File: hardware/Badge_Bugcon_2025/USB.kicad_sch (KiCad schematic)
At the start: 33 parts, among them J3 USB_A, J4 USB_A, J6 USB_A, P4 USB_C_Plug_USB2.0, Q1 DMG3415U-7, SW1 ON, SW4 SWITCH, U1 USB3740B-AI9, U3 SL2.1A, Y5 12MHz

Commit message: feat(Hw):Update_Schematic
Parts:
- removed BT1, BT2, BT3: Battery_Cell, Battery:BatteryHolder_Keystone_2466_1xAAA, symbol Device:Battery_Cell
- added C70, C71: 4.7uF, symbol Device:C
- added D16: D, symbol Device:D
- added J10: Conn_01x02, symbol Connector_Generic:Conn_01x02
- added R31: 2k, symbol Device:R
- added R32: 470, symbol Device:R
- added U5: MCP73831T-2ATI/OT, Package_TO_SOT_SMD:SOT-23-5, symbol Battery_Management:MCP73831-2-OT
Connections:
- net +5V: no longer SW4.1 (A), U1.5 (VDD)
- net +BATT: now also J10.1 (Pin_1)
- net GND: now also C70.1, C71.2, J10.2 (Pin_2), R31.2, U5.2 (V_{SS})
- net VBUS: now also D14.2 (A), D15.2 (A), SW4.1 (A), U1.5 (VDD), C70.2, D16.2 (A), U5.4 (V_{DD}); no longer D14.1 (K), D15.1 (K)
- net at F4.1: now also D15.1 (K); no longer D15.2 (A)
- net at F3.1: now also D14.1 (K); no longer D14.2 (A)
- new net: C71.1, U5.3 (V_{BAT})
- new net: R31.1, U5.5 (PROG)
- new net: D16.1 (K), R32.1
- new net STAT: R32.2, U5.1 (STAT)
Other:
- moved on the sheet: C18, C19, C55, C56, C57, D12, D14, D15, F3, F4, J4, J6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

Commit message: feat(Hw):Update_Schematic
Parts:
- C19, C55: footprint (none) -> Capacitor_SMD:C_0603_1608Metric; LCSC# (none) -> C96446
- C56, C57: footprint (none) -> Capacitor_SMD:C_0603_1608Metric
- C70, C71: footprint (none) -> Capacitor_SMD:C_0603_1608Metric; LCSC# (none) -> C162274
- D16: value D -> LED; footprint (none) -> LED_SMD:LED_0603_1608Metric; LCSC# (none) -> C375573
- J3, J4, J6: LCSC# (none) -> C18077686
- U3: LCSC# (none) -> C192893
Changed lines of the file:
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@@
 			)
 		)
-		(property "Value" "D"
+		(property "Value" "LED"
 			(at 262.89 73.6599 90)
 			(effects
@@
 			)
 		)
-		(property "Footprint" ""
+		(property "Footprint" "LED_SMD:LED_0603_1608Metric"
 			(at 260.35 72.39 0)
 			(effects
@@
 			)
 		)
+		(property "LCSC#" "C375573"
+			(at 260.35 72.39 90)
+			(effects
+				(font
+					(size 1.27 1.27)
+				)
+				(hide yes)
+			)
+		)
 		(pin "2"
 		)
@@
 			)
 		)
+		(property "LCSC#" "C18077686"
+			(at 27.94 116.84 0)
+			(effects
+				(font
+					(size 1.27 1.27)
+				)
+				(hide yes)
+			)
+		)
 		(pin "1"
 		)
@@
 			)
 		)
+		(property "LCSC#" "C192893"
+			(at 90.17 156.21 0)
+			(effects
+				(font
+					(size 1.27 1.27)
+				)
+				(hide yes)
+			)
+		)
 		(pin "7"
 		)
@@
 			)
 		)
-		(property "Footprint" ""
+		(property "Footprint" "Capacitor_SMD:C_0603_1608Metric"
 			(at 242.2652 82.55 0)
 			(effects
@@
 			)
 		)
+		(property "LCSC#" "C162274"
+			(at 241.3 78.74 0)
+			(effects
+				(font
+					(size 1.27 1.27)
+				)
+				(hide yes)
+			)
+		)
 		(pin "1"
 		)
@@
 			)
 		)
-		(property "Footprint" ""
+		(property "Footprint" "Capacitor_SMD:C_0603_1608Metric"
 			(at 63.8048 162.56 0)
 			(effects
@@
 			)
 		)
+		(property "LCSC#" "C96446"
+			(at 64.77 166.37 0)
+			(effects
+				(font
+					(size 1.27 1.27)
+				)
+				(hide yes)
+			)
+		)
 		(pin "2"
 		)
@@
 			)
 		)
-		(property "Footprint" ""
+		(property "Footprint" "Capacitor_SMD:C_0603_1608Metric"
 			(at 58.1152 170.18 0)
 			(effects
@@
 			)
 		)
+		(property "LCSC#" "C96446"
+			(at 57.15 166.37 0)
+			(effects
+				(font
+					(size 1.27 1.27)
+				)
+				(hide yes)
+			)
+		)
 		(pin "1"
 		)
@@
 			)
 		)
-		(property "Footprint" ""
+		(property "Footprint" "Capacitor_SMD:C_0603_1608Metric"
 			(at 159.7152 140.97 0)
 			(effects
@@
 			)
 		)
-		(property "Footprint" ""
+		(property "Footprint" "Capacitor_SMD:C_0603_1608Metric"
 			(at 210.82 62.5348 0)
 			(effects
@@
 			)
 		)
+		(property "LCSC#" "C162274"
+			(at 207.01 63.5 90)
+			(effects
+				(font
+					(size 1.27 1.27)
+				)
+				(hide yes)
+			)
+		)
 		(pin "1"
 		)
@@
 			)
 		)
-		(property "Footprint" ""
+		(property "Footprint" "Capacitor_SMD:C_0603_1608Metric"
 			(at 160.9852 173.99 0)
 			(effects
@@
 			)
 		)
+		(property "LCSC#" "C18077686"
+			(at 144.78 137.16 0)
+			(effects
+				(font
+					(size 1.27 1.27)
+				)
+				(hide yes)
+			)
+		)
 		(pin "1"
 		)
@@
 			(at 144.78 170.18 0)
 			(effects
+				(font
+					(size 1.27 1.27)
+				)
+				(hide yes)
+			)
+		)
+		(property "LCSC#" "C18077686"
+			(at 144.78 170.18 0)
+			(effects

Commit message: feat(Hw):Update_BOM
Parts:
- removed SW4: SWITCH, symbol Switch:SW_SPDT
- added SW4: On, Footprints:MSK12C02, symbol Switch:SW_DPDT_x2
- C56, C57: footprint Capacitor_SMD:C_0603_1608Metric -> Capacitor_SMD:C_0805_2012Metric; LCSC# (none) -> C141660
- J3, J4, J6: footprint (none) -> Connector_USB:USB_A_Connfly_DS1095
- R31: footprint (none) -> LED_SMD:LED_0603_1608Metric; LCSC# (none) -> C2907022
- R32: footprint (none) -> LED_SMD:LED_0603_1608Metric; LCSC# (none) -> C23179
- U1: footprint (none) -> Package_DFN_QFN:UQFN-10_1.3x1.8mm_P0.4mm
- U3: footprint (none) -> Package_SO:SOP-16_3.9x9.9mm_P1.27mm
- Y5: footprint Crystal:Crystal_SMD_3215-2Pin_3.2x1.5mm -> Crystal:Crystal_SMD_3225-4Pin_3.2x2.5mm; LCSC# C620155 -> C133334
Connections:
- net GND: now also SW4.3 (C), SW4.4 (C)
- net S: now also SW4.2 (B)
- net VBUS: now also SW4.1 (A)
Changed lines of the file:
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@@
 	)
 	(junction
+		(at 165.1 49.53)
+		(diameter 0)
+		(color 0 0 0 0)
+	)
+	(junction
 		(at 146.05 181.61)
 		(diameter 0)
@@
 	(wire
 		(pts
+			(xy 162.56 45.72) (xy 165.1 45.72)
+		)
+		(stroke
+			(width 0)
+			(type default)
+		)
+	)
+	(wire
+		(pts
 			(xy 215.9 83.82) (xy 215.9 85.09)
 		)
@@
 	(wire
 		(pts
+			(xy 165.1 45.72) (xy 165.1 49.53)
+		)
+		(stroke
+			(width 0)
+			(type default)
+		)
+	)
+	(wire
+		(pts
 			(xy 135.89 132.08) (xy 137.16 132.08)
 		)
@@
 	(wire
 		(pts
-			(xy 165.1 45.72) (xy 162.56 45.72)
+			(xy 165.1 49.53) (xy 162.56 49.53)
 		)
 		(stroke
@@
 	(wire
 		(pts
-			(xy 165.1 46.99) (xy 165.1 45.72)
+			(xy 165.1 52.07) (xy 165.1 49.53)
 		)
 		(stroke
@@
 	(symbol
 		(lib_id "power:GND")
-		(at 165.1 46.99 0)
+		(at 165.1 52.07 0)
 		(unit 1)
 		(exclude_from_sim no)
@@
 		(dnp no)
 		(property "Reference" "#PWR086"
-			(at 165.1 53.34 0)
+			(at 165.1 58.42 0)
 			(effects
 				(font
@@
 		)
 		(property "Value" "GND"
-			(at 165.227 51.3842 0)
+			(at 165.227 56.4642 0)
 			(effects
 				(font
@@
 		)
 		(property "Footprint" ""
-			(at 165.1 46.99 0)
+			(at 165.1 52.07 0)
 			(effects
 				(font
@@
 		)
 		(property "Datasheet" ""
-			(at 165.1 46.99 0)
+			(at 165.1 52.07 0)
 			(effects
 				(font
@@
 		)
 		(property "Description" ""
-			(at 165.1 46.99 0)
+			(at 165.1 52.07 0)
 			(effects
 				(font
@@
 			)
 		)
-		(property "Footprint" ""
+		(property "Footprint" "Connector_USB:USB_A_Connfly_DS1095"
 			(at 31.75 118.11 0)
 			(effects
@@
 			)
 		)
-		(property "Footprint" ""
+		(property "Footprint" "Package_SO:SOP-16_3.9x9.9mm_P1.27mm"
 			(at 90.17 156.21 0)
 			(effects
@@
 			)
 		)
-		(property "Footprint" ""
+		(property "Footprint" "Package_DFN_QFN:UQFN-10_1.3x1.8mm_P0.4mm"
 			(at 90.17 49.53 0)
 			(effects
@@
 			)
 		)
-		(property "Footprint" ""
+		(property "Footprint" "LED_SMD:LED_0603_1608Metric"
 			(at 258.572 81.28 90)
 			(effects
@@
 			)
 		)
+		(property "LCSC#" "C23179"
+			(at 260.35 81.28 0)
+			(effects
+				(font
+					(size 1.27 1.27)
+				)
+				(hide yes)
+			)
+		)
 		(pin "2"
 		)
@@
 	)
 	(symbol
+		(lib_id "Switch:SW_DPDT_x2")
+		(at 157.48 43.18 0)
+		(unit 1)
+		(exclude_from_sim no)
+		(in_bom yes)
+		(on_board yes)
+		(dnp no)
+		(property "Reference" "SW4"
+			(at 155.702 46.609 0)
+			(effects
+				(font
+					(size 1.27 1.27)
+				)
+			)
+		)
+		(property "Value" "On"
+			(at 157.48 38.2524 0)
+			(effects
+				(font
+					(size 1.27 1.27)
+				)
+			)
+		)
+		(property "Footprint" "Footprints:MSK12C02"
+			(at 157.48 43.18 0)
+			(effects
+				(font
+					(size 1.27 1.27)
+				)
+				(hide yes)
+			)
+		)
+		(property "Datasheet" "~"
+			(at 157.48 43.18 0)
+			(effects
+				(font
+					(size 1.27 1.27)
+				)
+				(hide yes)
+			)
+		)
+		(property "Description" ""
+			(at 157.48 43.18 0)
+			(effects
+				(font
+					(size 1.27 1.27)
+				)
+				(hide yes)
+			)
+		)
+		(property "LCSC#" "C431540"
+			(at 157.48 43.18 0)
+			(effects
+				(font
+					(size 1.27 1.27)
+				)
+				(hide yes)
+			)
+		)
+		(property "manf#" ""
+			(at 157.48 43.18 0)
+			(effects
+				(font
+					(size 1.27 1.27)
+				)
+				(hide yes)
+			)
+		)
+		(pin "1"
+		)
+		(pin "2"
+		)
+		(pin "3"
+		)
+		(pin "4"
+		)
+		(pin "5"
+		)
+		(pin "6"
+		)
+		(pin "4"
+		)
+		(instances
+			(project "Badge_Bugcon_2025"
+				(path "/a95785a0-0aa1-454e-b59f-0ac64970ac71/a5c26cac-72fa-4752-a660-9cd751934916"
+					(reference "SW4")
+					(unit 1)
+				)
+			)
+		)
+	)
+	(symbol
 		(lib_id "power:GND")
 		(at 49.53 157.48 0)
@@
 	)
 	(symbol
-		(lib_id "Switch:SW_SPDT")
-		(at 157.48 43.18 0)
-		(unit 1)
-		(exclude_from_sim no)
-		(in_bom yes)
-		(on_board yes)
-		(dnp no)
-		(fields_autoplaced yes)
-		(property "Reference" "SW4"
-			(at 157.48 34.29 0)
-			(effects
-				(font
-					(size 1.27 1.27)
-				)
-			)
-		)
-		(property "Value" "SWITCH"
-			(at 157.48 36.83 0)
-			(effects
-				(font
-					(size 1.27 1.27)
-				)
-			)
-		)
-		(property "Footprint" ""
-			(at 157.48 43.18 0)
-			(effects
-				(font
-					(size 1.27 1.27)
-				)
-				(hide yes)
-			)
-		)
-		(property "Datasheet" "~"
-			(at 157.48 50.8 0)
-			(effects
-				(font
-					(size 1.27 1.27)
-				)
-				(hide yes)
-			)
-		)
-		(property "Description" "Switch, single pole double throw"
-			(at 157.48 43.18 0)
-			(effects
-				(font
-					(size 1.27 1.27)
-				)
-				(hide yes)
-			)
-		)
-		(property "Height" ""
-			(at 157.48 43.18 0)
-			(effects
-				(font
-					(size 1.27 1.27)
-				)
-				(hide yes)
-			)
-		)
-		(property "Manufacturer_Name" ""
-			(at 157.48 43.18 0)
-			(effects
-				(font
-					(size 1.27 1.27)
-				)
-				(hide yes)
-			)
-		)
-		(property "Mouser Part Number" ""
-			(at 157.48 43.18 0)
-			(effects
-				(font
-					(size 1.27 1.27)
-				)
-				(hide yes)
-			)
-		)
-		(property "Mouser Price/Stock" ""
-			(at 157.48 43.18 0)
-			(effects
-				(font
-					(size 1.27 1.27)
-				)
-				(hide yes)
-			)
-		)
-		(pin "3"
-		)
-		(pin "1"
-		)
-		(pin "2"
-		)
-		(instances
-			(project ""
-				(path "/a95785a0-0aa1-454e-b59f-0ac64970ac71/a5c26cac-72fa-4752-a660-9cd751934916"
-					(reference "SW4")
-					(unit 1)
-				)
-			)
-		)
-	)
-	(symbol
 		(lib_id "power:+5V")
 		(at 243.84 139.7 0)
@@
 			)
 		)
-		(property "Footprint" "Capacitor_SMD:C_0603_1608Metric"
+		(property "Footprint" "Capacitor_SMD:C_0805_2012Metric"
 			(at 159.7152 140.97 0)
 			(effects
@@
 			)
 		)
+		(property "LCSC#" "C141660"
+			(at 158.75 137.16 0)
+			(effects
+				(font
+					(size 1.27 1.27)
+				)
+				(hide yes)
+			)
+		)
 		(pin "1"
 		)
@@
 			)
 		)
-		(property "Footprint" "Capacitor_SMD:C_0603_1608Metric"
+		(property "Footprint" "Capacitor_SMD:C_0805_2012Metric"
 			(at 160.9852 173.99 0)
 			(effects
@@
 			)
 		)
+		(property "LCSC#" "C141660"
+			(at 160.02 170.18 0)
+			(effects
+				(font
+					(size 1.27 1.27)
+				)
+				(hide yes)
+			)
+		)
 		(pin "1"
 		)
@@
 			)
 		)
-		(property "Footprint" ""
+		(property "Footprint" "Connector_USB:USB_A_Connfly_DS1095"
 			(at 140.97 138.43 0)
 			(effects
@@
 			)
 		)
-		(property "Footprint" ""
+		(property "Footprint" "LED_SMD:LED_0603_1608Metric"
 			(at 197.612 83.82 90)
 			(effects
@@
 			)
 		)
+		(property "LCSC#" "C2907022"
+			(at 199.39 83.82 0)
+			(effects
+				(font
+					(size 1.27 1.27)
+				)
+				(hide yes)
+			)
+		)
 		(pin "1"
 		)
@@
 			)
 		)
-		(property "Footprint" ""
+		(property "Footprint" "Connector_USB:USB_A_Connfly_DS1095"
 			(at 140.97 171.45 0)
 			(effects
@@
 			)
 		)
-		(property "Footprint" "Crystal:Crystal_SMD_3215-2Pin_3.2x1.5mm"
+		(property "Footprint" "Crystal:Crystal_SMD_3225-4Pin_3.2x2.5mm"
 			(at 83.82 184.15 0)
 			(effects
@@
 			)
 		)
-		(property "LCSC#" "C620155"
+		(property "LCSC#" "C133334"
 			(at 83.82 184.15 0)
 			(effects

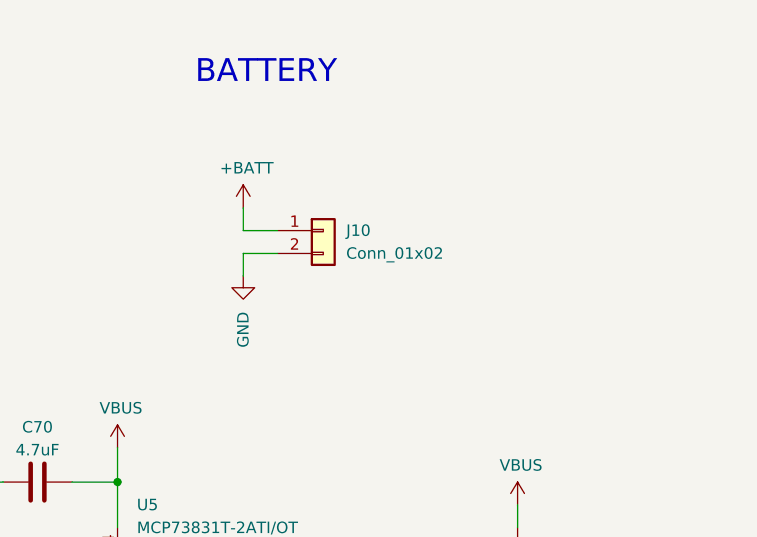
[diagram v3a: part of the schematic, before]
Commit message: feat(Hw):Update_Schematic_And_Floorplan
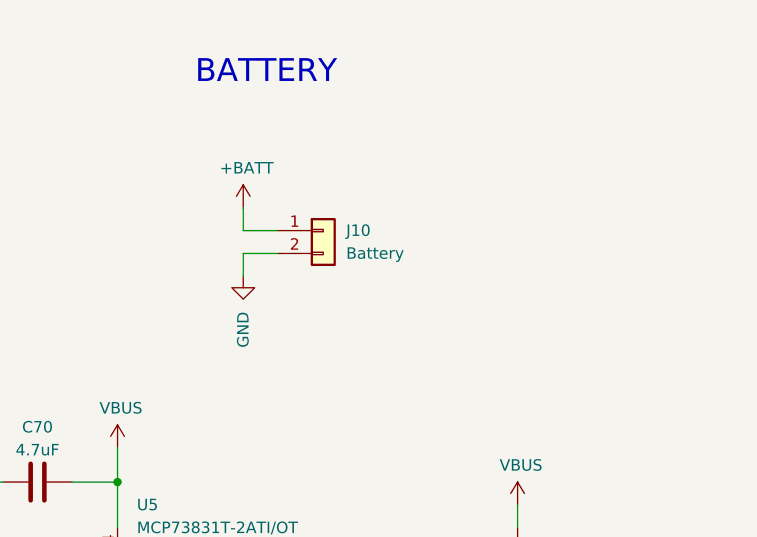
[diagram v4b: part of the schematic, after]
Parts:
- J10: value Conn_01x02 -> Battery; footprint (none) -> Footprints:Batt; LCSC# (none) -> C131337
- SW1: footprint FootprintsB:SW-TH_SK12D07VG4 -> Button_Switch_THT:SW_Slide_SPDT_Angled_CK_OS102011MA1Q
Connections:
- net XIN: now also Y5.3; no longer Y5.2
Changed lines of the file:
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@@
 			)
 		)
-		(property "Value" "Conn_01x02"
+		(property "Value" "Battery"
 			(at 241.3 38.0999 0)
 			(effects
@@
 			)
 		)
-		(property "Footprint" ""
+		(property "Footprint" "Footprints:Batt"
 			(at 238.76 35.56 0)
 			(effects
@@
 			)
 		)
-		(property "Datasheet" "https://uelectronics.com/producto/bateria-lipo-3-7v-2500mah/"
+		(property "Datasheet" ""
 			(at 238.76 35.56 0)
 			(effects
@@
 			)
 		)
+		(property "LCSC#" "C131337"
+			(at 238.76 35.56 0)
+			(effects
+				(font
+					(size 1.27 1.27)
+				)
+				(hide yes)
+			)
+		)
 		(pin "2"
 		)
@@
 			)
 		)
-		(property "Footprint" "FootprintsB:SW-TH_SK12D07VG4"
+		(property "Footprint" "Button_Switch_THT:SW_Slide_SPDT_Angled_CK_OS102011MA1Q"
 			(at 229.87 142.24 0)
 			(effects
@@
 		(pin "1"
 		)
-		(pin "2"
+		(pin "3"
 		)
 		(instances

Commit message: feat(Hw):Update_Schematic
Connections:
- net +BATT: now also C71.1, U5.3 (V_{BAT})
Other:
- note added: "BATTERY CHARGER"
- note added: "USB SELECTOR"
- note removed: "BATTERY"
- moved on the sheet: C18, C19, C54, C55, C56, C57, C70, C71, D12, D13, D14, D15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

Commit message: feat(Hw):Update_Schematic
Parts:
- removed U5: MCP73831T-2ATI/OT, Package_TO_SOT_SMD:SOT-23-5, symbol Battery_Management:MCP73831-2-OT
- added D8: LED, LED_SMD:LED_0603_1608Metric, symbol Device:D
- added U2: TP4056, Package_SO:SOIC-8-1EP_3.9x4.9mm_P1.27mm_EP2.41x3.3mm_ThermalVias, symbol Battery_Management:TP4056-42-ESOP8
- C70, C71: value 4.7uF -> 10uF
- R32: value 470 -> 10K; footprint LED_SMD:LED_0603_1608Metric -> Resistor_SMD:R_0402_1005Metric; LCSC# C23179 -> C2759535
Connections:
- net STAT is gone; now on net GND: R32.2
- net +BATT: now also U2.5 (BAT)
- net GND: now also U2.3 (GND), U2.9 (EPAD); no longer R31.2
- net VBUS: now also R31.1, U2.4 (V_{CC}); no longer D16.2 (A)
- net at D16.1 (K): now also U2.7 (~{CHRG}); no longer R32.1
- new net: D16.2 (A), D8.2 (A), R31.2
- new net: R32.1, U2.2 (PROG)
- new net: D8.1 (K), U2.6 (~{STDBY})
- no-connect marks 4 -> 5
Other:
- moved on the sheet: C70, C71, D16, R31

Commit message: feat(Hw):Update_Schematic
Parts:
- C70, C71: LCSC# C162274 -> C96446
- J10: LCSC# C131337 -> C2988620; manf# Bateria LiPo 3.7V 2500mAh 104050 -> Bateria 18650 3.7V 2200mAh ±5%
- U2: LCSC# (none) -> C725790
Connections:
- net VBUS: now also U2.8 (CE)
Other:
- moved on the sheet: C70
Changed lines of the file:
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@@
 	)
 	(junction
-		(at 218.44 48.26)
+		(at 218.44 44.45)
 		(diameter 0)
 		(color 0 0 0 0)
@@
 	)
 	(junction
+		(at 218.44 52.07)
+		(diameter 0)
+		(color 0 0 0 0)
+	)
+	(junction
 		(at 186.69 66.04)
 		(diameter 0)
@@
 	(wire
 		(pts
-			(xy 213.36 48.26) (xy 218.44 48.26)
+			(xy 213.36 44.45) (xy 218.44 44.45)
 		)
 		(stroke
@@
 	(wire
 		(pts
-			(xy 205.74 48.26) (xy 203.2 48.26)
+			(xy 205.74 44.45) (xy 203.2 44.45)
 		)
 		(stroke
@@
 	(wire
 		(pts
+			(xy 218.44 52.07) (xy 218.44 53.34)
+		)
+		(stroke
+			(width 0)
+			(type default)
+		)
+	)
+	(wire
+		(pts
 			(xy 142.24 22.86) (xy 143.51 22.86)
 		)
@@
 	(wire
 		(pts
-			(xy 218.44 44.45) (xy 218.44 48.26)
+			(xy 218.44 39.37) (xy 218.44 44.45)
 		)
 		(stroke
@@
 	(wire
 		(pts
-			(xy 218.44 48.26) (xy 218.44 53.34)
+			(xy 218.44 44.45) (xy 218.44 52.07)
 		)
 		(stroke
@@
 	(wire
 		(pts
-			(xy 203.2 48.26) (xy 203.2 50.8)
+			(xy 203.2 44.45) (xy 203.2 46.99)
 		)
 		(stroke
@@
 	(wire
 		(pts
+			(xy 205.74 52.07) (xy 218.44 52.07)
+		)
+		(stroke
+			(width 0)
+			(type default)
+		)
+	)
+	(wire
+		(pts
 			(xy 38.1 36.83) (xy 40.64 36.83)
 		)
@@
 	(wire
 		(pts
+			(xy 208.28 60.96) (xy 205.74 60.96)
+		)
+		(stroke
+			(width 0)
+			(type default)
+		)
+	)
+	(wire
+		(pts
 			(xy 52.07 151.13) (xy 55.88 151.13)
 		)
@@
 	(wire
 		(pts
+			(xy 205.74 60.96) (xy 205.74 52.07)
+		)
+		(stroke
+			(width 0)
+			(type default)
+		)
+	)
+	(wire
+		(pts
 			(xy 156.21 114.3) (xy 156.21 115.57)
 		)
@@
 			)
 		)
-		(property "manf#" "Bateria LiPo 3.7V 2500mAh 104050"
+		(property "manf#" "Bateria 18650 3.7V 2200mAh ±5% "
 			(at 274.32 60.96 0)
 			(effects
@@
 			)
 		)
-		(property "LCSC#" "C131337"
+		(property "LCSC#" "C2988620"
 			(at 274.32 60.96 0)
 			(effects
@@
 			)
 		)
-		(property "Datasheet" "https://www.lcsc.com/datasheet/lcsc_datasheet_2410121619_TOPPOWER-Nanjing-Extension-Microelectronics-TP4056-42-ESOP8_C16581.pdf"
+		(property "Datasheet" "https://www.lcsc.com/datasheet/C725790.pdf"
 			(at 218.44 91.44 0)
 			(effects
@@
 			)
 		)
+		(property "LCSC#" "C725790"
+			(at 218.44 66.04 0)
+			(effects
+				(font
+					(size 1.27 1.27)
+				)
+				(hide yes)
+			)
+		)
 		(pin "3"
 		)
@@
 	(symbol
 		(lib_id "power:GND")
-		(at 203.2 50.8 0)
+		(at 203.2 46.99 0)
 		(unit 1)
 		(exclude_from_sim no)
@@
 		(dnp no)
 		(property "Reference" "#PWR0161"
-			(at 203.2 57.15 0)
+			(at 203.2 53.34 0)
 			(effects
 				(font
@@
 		)
 		(property "Value" "GND"
-			(at 205.232 54.61 0)
+			(at 205.232 50.8 0)
 			(effects
 				(font
@@
 		)
 		(property "Footprint" ""
-			(at 203.2 50.8 0)
+			(at 203.2 46.99 0)
 			(effects
 				(font
@@
 		)
 		(property "Datasheet" ""
-			(at 203.2 50.8 0)
+			(at 203.2 46.99 0)
 			(effects
 				(font
@@
 		)
 		(property "Description" ""
-			(at 203.2 50.8 0)
+			(at 203.2 46.99 0)
 			(effects
 				(font
@@
 	(symbol
 		(lib_id "power:VBUS")
-		(at 218.44 44.45 0)
+		(at 218.44 39.37 0)
 		(unit 1)
 		(exclude_from_sim no)
@@
 		(dnp no)
 		(property "Reference" "#PWR030"
-			(at 218.44 48.26 0)
+			(at 218.44 43.18 0)
 			(effects
 				(font
@@
 		)
 		(property "Value" "VBUS"
-			(at 218.821 40.0558 0)
+			(at 218.821 34.9758 0)
 			(effects
 				(font
@@
 		)
 		(property "Footprint" ""
-			(at 218.44 44.45 0)
+			(at 218.44 39.37 0)
 			(effects
 				(font
@@
 		)
 		(property "Datasheet" ""
-			(at 218.44 44.45 0)
+			(at 218.44 39.37 0)
 			(effects
 				(font
@@
 		)
 		(property "Description" ""
-			(at 218.44 44.45 0)
+			(at 218.44 39.37 0)
 			(effects
 				(font
@@
 			)
 		)
-		(property "LCSC#" "C162274"
+		(property "LCSC#" "C96446"
 			(at 243.84 66.04 0)
 			(effects
@@
 	(symbol
 		(lib_id "Device:C")
-		(at 209.55 48.26 90)
+		(at 209.55 44.45 90)
 		(unit 1)
 		(exclude_from_sim no)
@@
 		(dnp no)
 		(property "Reference" "C70"
-			(at 209.55 42.164 90)
+			(at 209.55 38.354 90)
 			(effects
 				(font
@@
 		)
 		(property "Value" "10uF"
-			(at 209.55 44.704 90)
+			(at 209.55 40.894 90)
 			(effects
 				(font
@@
 		)
 		(property "Footprint" "Capacitor_SMD:C_0603_1608Metric"
-			(at 213.36 47.2948 0)
+			(at 213.36 43.4848 0)
 			(effects
 				(font
@@
 		)
 		(property "Datasheet" "~"
-			(at 209.55 48.26 0)
+			(at 209.55 44.45 0)
 			(effects
 				(font
@@
 		)
 		(property "Description" "Unpolarized capacitor"
-			(at 209.55 48.26 0)
+			(at 209.55 44.45 0)
 			(effects
 				(font
@@
 		)
 		(property "Height" ""
-			(at 209.55 48.26 90)
+			(at 209.55 44.45 90)
 			(effects
 				(font
@@
 		)
 		(property "Manufacturer_Name" ""
-			(at 209.55 48.26 90)
+			(at 209.55 44.45 90)
 			(effects
 				(font
@@
 		)
 		(property "Mouser Part Number" ""
-			(at 209.55 48.26 90)
+			(at 209.55 44.45 90)
 			(effects
 				(font
@@
 		)
 		(property "Mouser Price/Stock" ""
-			(at 209.55 48.26 90)
+			(at 209.55 44.45 90)
 			(effects
 				(font
@@
 			)
 		)
-		(property "LCSC#" "C162274"
-			(at 209.55 48.26 90)
+		(property "LCSC#" "C96446"
+			(at 209.55 44.45 90)
 			(effects
 				(font
@@
 		)
 		(property "Availability" ""
-			(at 209.55 48.26 90)
+			(at 209.55 44.45 90)
 			(effects
 				(font
@@
 		)
 		(property "Check_prices" ""
-			(at 209.55 48.26 90)
+			(at 209.55 44.45 90)
 			(effects
 				(font
@@
 		)
 		(property "Description_1" ""
-			(at 209.55 48.26 90)
+			(at 209.55 44.45 90)
 			(effects
 				(font
@@
 		)
 		(property "MANUFACTURER" ""
-			(at 209.55 48.26 90)
+			(at 209.55 44.45 90)
 			(effects
 				(font
@@
 		)
 		(property "MAXIMUM_PACKAGE_HEIGHT" ""
-			(at 209.55 48.26 90)
+			(at 209.55 44.45 90)
 			(effects
 				(font
@@
 		)
 		(property "MF" ""
-			(at 209.55 48.26 90)
+			(at 209.55 44.45 90)
 			(effects
 				(font
@@
 		)
 		(property "MP" ""
-			(at 209.55 48.26 90)
+			(at 209.55 44.45 90)
 			(effects
 				(font
@@
 		)
 		(property "PARTREV" ""
-			(at 209.55 48.26 90)
+			(at 209.55 44.45 90)
 			(effects
 				(font
@@
 		)
 		(property "Package" ""
-			(at 209.55 48.26 90)
+			(at 209.55 44.45 90)
 			(effects
 				(font
@@
 		)
 		(property "Price" ""
-			(at 209.55 48.26 90)
+			(at 209.55 44.45 90)
 			(effects
 				(font
@@
 		)
 		(property "STANDARD" ""
-			(at 209.55 48.26 90)
+			(at 209.55 44.45 90)
 			(effects
 				(font
@@
 		)
 		(property "SnapEDA_Link" ""
-			(at 209.55 48.26 90)
+			(at 209.55 44.45 90)
 			(effects
 				(font
